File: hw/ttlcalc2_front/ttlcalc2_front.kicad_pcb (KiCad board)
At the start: 2 copper layers, 330.2 x 76.2 mm, 61 parts, among them J1 DISP_CONN, J2 PWR_HV

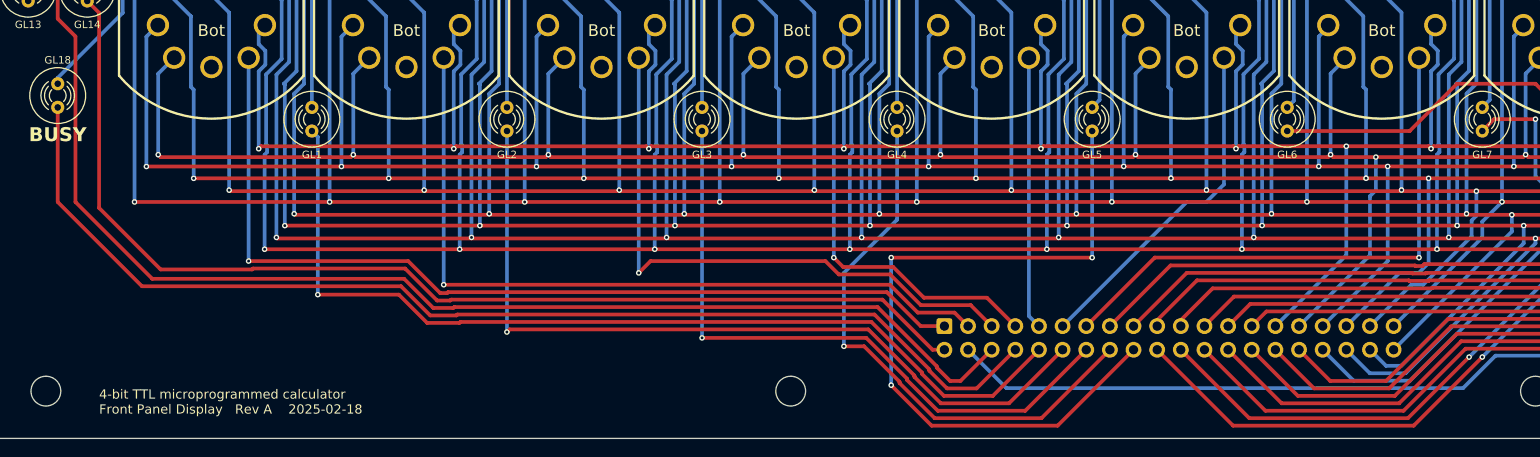
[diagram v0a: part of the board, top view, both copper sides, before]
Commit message: Minor routing tweaks to front panel display
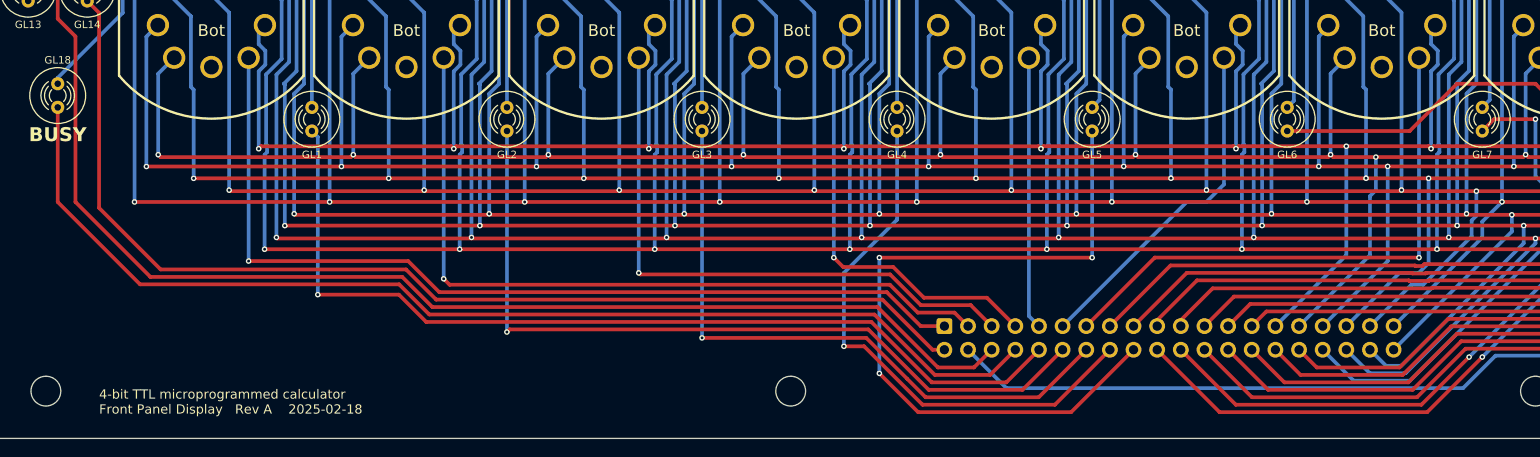
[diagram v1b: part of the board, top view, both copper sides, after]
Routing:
- net NE_ERR: track 143.0 -> 141.7 mm
- net NE_BUSY: track 123.2 -> 121.8 mm
- net DP_0: track 102.0 -> 100.7 mm
- net DP_1: track 87.2 -> 85.9 mm
- net DP_2: track 69.5 -> 68.3 mm
- net DP_3: track 60.4 -> 59.1 mm
- net DP_7: track 79.8 -> 78.6 mm
- net DP_10: track 131.7 -> 130.4 mm
- net DP_9: track 114.4 -> 113.2 mm
- net DP_6: track 73.3 -> 72.1 mm
- net DP_5: track 104.5 -> 103.3 mm
- net DP_11: track 148.8 -> 147.6 mm
- net DP_8: track 97.1 -> 95.9 mm
- net NXA_2: track 64.4 -> 63.4 mm
- net DP_4: track 80.1 -> 80.7 mm
